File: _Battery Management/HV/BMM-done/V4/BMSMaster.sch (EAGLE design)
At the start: 119 parts, among them J1 M2_DF13-2P, J10 IMD, J14 USB_B_RA, J2 M2_DF13-2P, J3 M8S08B-PASK-2(LF)(SN), J5 M16_M_194280016, J6 M2770166, J7 M2770166, J8 M2770166, J9 M2770166, K1 ADJ14024, Q1 IRFR9120TRPBF, Q3 BSS123, U1 SN75HVD08DRMSOP, U10 NC7S14M5X, U11 LTC6820, U12 FT24C64A, U2 NCP1117DT_3.3, U22 NCV7805BDTRKG, U23 NUD3160DMT1G, U3 FT230X, U4 SN74LVC2G241, U5 NC7S14M5X, U6 DSPIC33FJ128GP804, U7 DMG6602SVTQ, U8 LTC6820, U9 MAX823TEUK+T_3.08, Y1 12Mhz

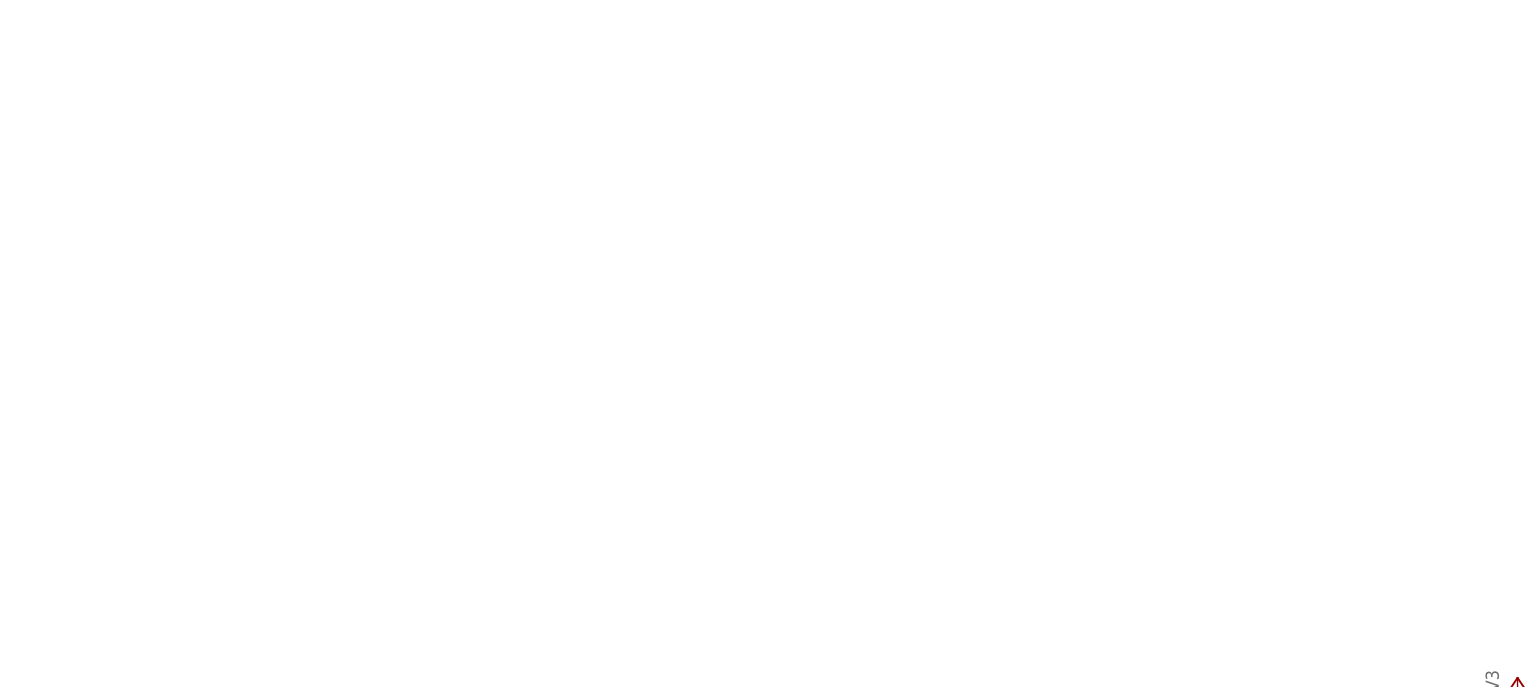
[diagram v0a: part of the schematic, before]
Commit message: Routing/ changing power supply
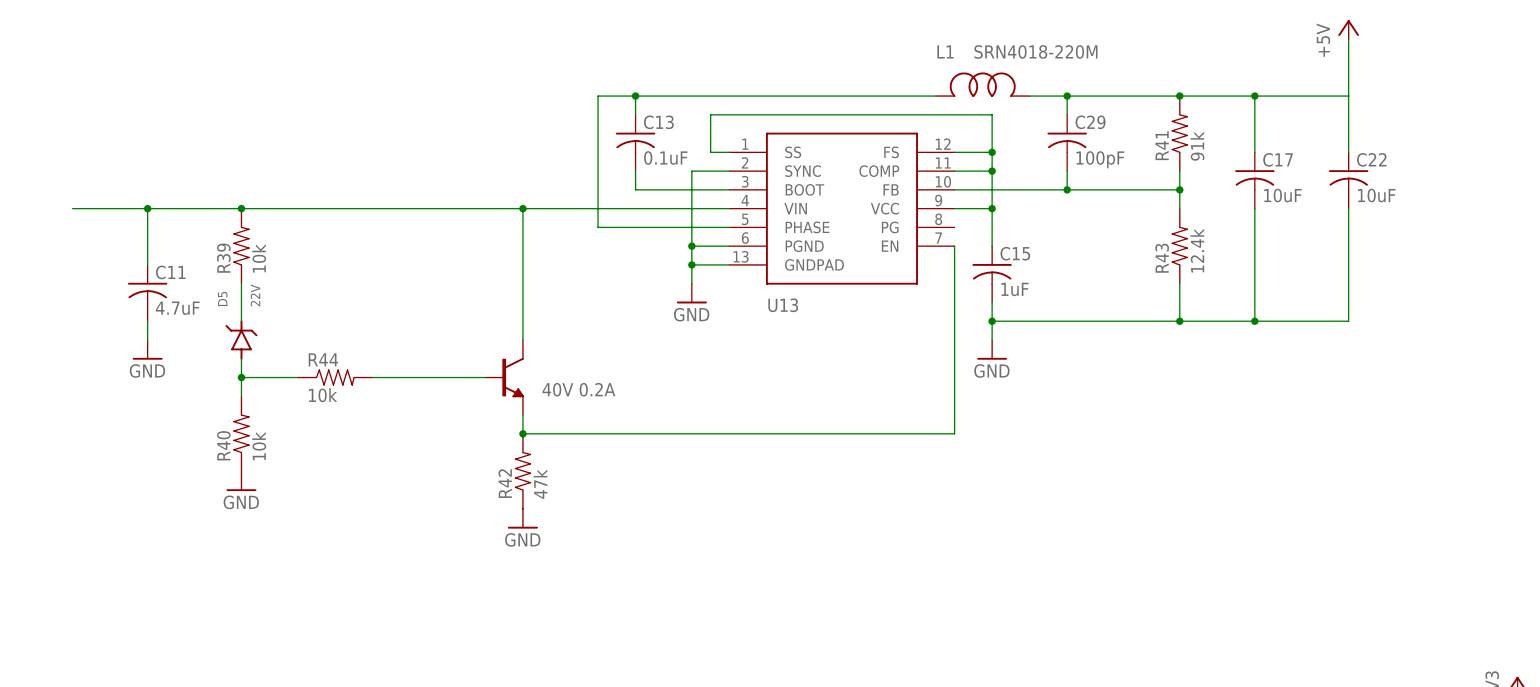
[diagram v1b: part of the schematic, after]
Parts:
- added C11: 4.7uF, FSAE Electric:CAP_4.7UF_50V
- added C13: 0.1uF, FSAE Electric:CAP_0.1UF_50V
- added C15: 1uF, FSAE Electric:CAP_1UF_50V_0805
- added C17, C22: 10uF, FSAE Electric:CAP_10UF_50V
- added C29: 100pF, FSAE Electric:CAP_100PF_50V
- added D5: 22V, FSAE Electric:DIODE-ZENER_22V
- added L1: SRN4018-220M, FSAE Electric:SRN4018-220M
- added Q2: 40V 0.2A, FSAE Electric:NPN_40V_0.2A
- added R39, R40, R44: 10k, FSAE Electric:RES_10K_1%
- added R41: 91k, FSAE Electric:RES_91K_1%_0805
- added R42: 47k, FSAE Electric:RES_47K_1%
- added R43: 12.4k, FSAE Electric:RES_12.4K_1%
- added U13: ISL85415-FRZ-T7A, FSAE Electric:ISL85415-FRZ-T7A
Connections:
- new net N$21: D5.A, R40.2, R44.1
- new net N$52: Q2.P$2, R42.2, U13.EN
- new net N$53: D5.C, R39.1
- new net N$55: C13.+, L1.P$1, U13.PHASE
- new net N$56: C13.-, U13.BOOT
- new net N$57: C15.+, U13.COMP, U13.FS, U13.SS, U13.VCC
- new net N$58: Q2.P$1, R44.2
- new net N$59: C11.+, Q2.P$3, R39.2, U13.VIN
- new net N$66: C29.-, R41.1, R43.2, U13.FB
- net +5V: now also C17.+, C22.+, C29.+, L1.P$2, R41.2
- net GND: now also C11.-, C15.-, C17.-, C22.-, R40.1, R42.1, R43.1, U13.GNDPAD, U13.PGND, U13.SYNC

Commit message: Trying to figure out DC/DC converter
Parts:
- removed C11: 4.7uF, FSAE Electric:CAP_4.7UF_50V
- removed C13: 0.1uF, FSAE Electric:CAP_0.1UF_50V
- removed C15: 1uF, FSAE Electric:CAP_1UF_50V_0805
- removed C17, C22: 10uF, FSAE Electric:CAP_10UF_50V
- removed C27, C28, C5, C6: 10UF, FSAE Electric:CAP-POL_10UF_16V
- removed C29: 100pF, FSAE Electric:CAP_100PF_50V
- removed D5: 22V, FSAE Electric:DIODE-ZENER_22V
- removed L1: SRN4018-220M, FSAE Electric:SRN4018-220M
- removed Q2: 40V 0.2A, FSAE Electric:NPN_40V_0.2A
- removed R39, R40, R44: 10k, FSAE Electric:RES_10K_1%
- removed R41: 91k, FSAE Electric:RES_91K_1%_0805
- removed R42: 47k, FSAE Electric:RES_47K_1%
- removed R43: 12.4k, FSAE Electric:RES_12.4K_1%
- removed U13: ISL85415-FRZ-T7A, FSAE Electric:ISL85415-FRZ-T7A
- removed U2: NCP1117DT_3.3, FSAE Electric:NCP1117DT_3.3
- removed U22: NCV7805BDTRKG, FSAE Electric:NCV7805BDTRKG
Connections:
- removed net N$21: D5.A, R40.2, R44.1
- removed net N$52: Q2.P$2, R42.2, U13.EN
- removed net N$53: D5.C, R39.1
- removed net N$55: C13.+, L1.P$1, U13.PHASE
- removed net N$56: C13.-, U13.BOOT
- removed net N$57: C15.+, U13.COMP, U13.FS, U13.SS, U13.VCC
- removed net N$58: Q2.P$1, R44.2
- removed net N$59: C11.+, Q2.P$3, R39.2, U13.VIN
- removed net N$66: C29.-, R41.1, R43.2, U13.FB
- new net N$60: L3.1
- net +3V3: no longer C28.+, U2.OUT
- net +5V: no longer C17.+, C22.+, C27.+, C29.+, L1.P$2, R41.2, U22.VO
- net +9V: no longer C5.+, C6.+, U2.IN, U22.VI
- net GND: no longer C11.-, C15.-, C17.-, C22.-, C27.-, C28.-, C5.-, C6.-, L3.1, R40.1, R42.1, R43.1, U13.GNDPAD, U13.PGND, U13.SYNC, U2.GND, U22.GND

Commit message: Adding parts and still routing
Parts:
- J1, J2: value M2_DF13-2P -> M2S02B-PASK-2(LF)(SN); device FSAE Electric:M2_DF13-2P -> FSAE Electric:M2S02B-PASK-2(LF)(SN)
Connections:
- removed net N$31: J5.6, K1G$2.C
- removed net N$32: J5.7, K1G$2.NC
- removed net N$59_N: J1.2, TX4.4
- removed net N$61_N: J2.2, TX3.4
- new net N$21: J5.6
- new net N$52: J5.7
- new net N$53: J2.2, TX4.6
- new net N$55: J2.1, TX4.4
- net N$33: now also J1.2, TX3.6; no longer J1.1, TX4.6
- net N$34: now also J1.1, TX3.4; no longer J2.1, TX3.6

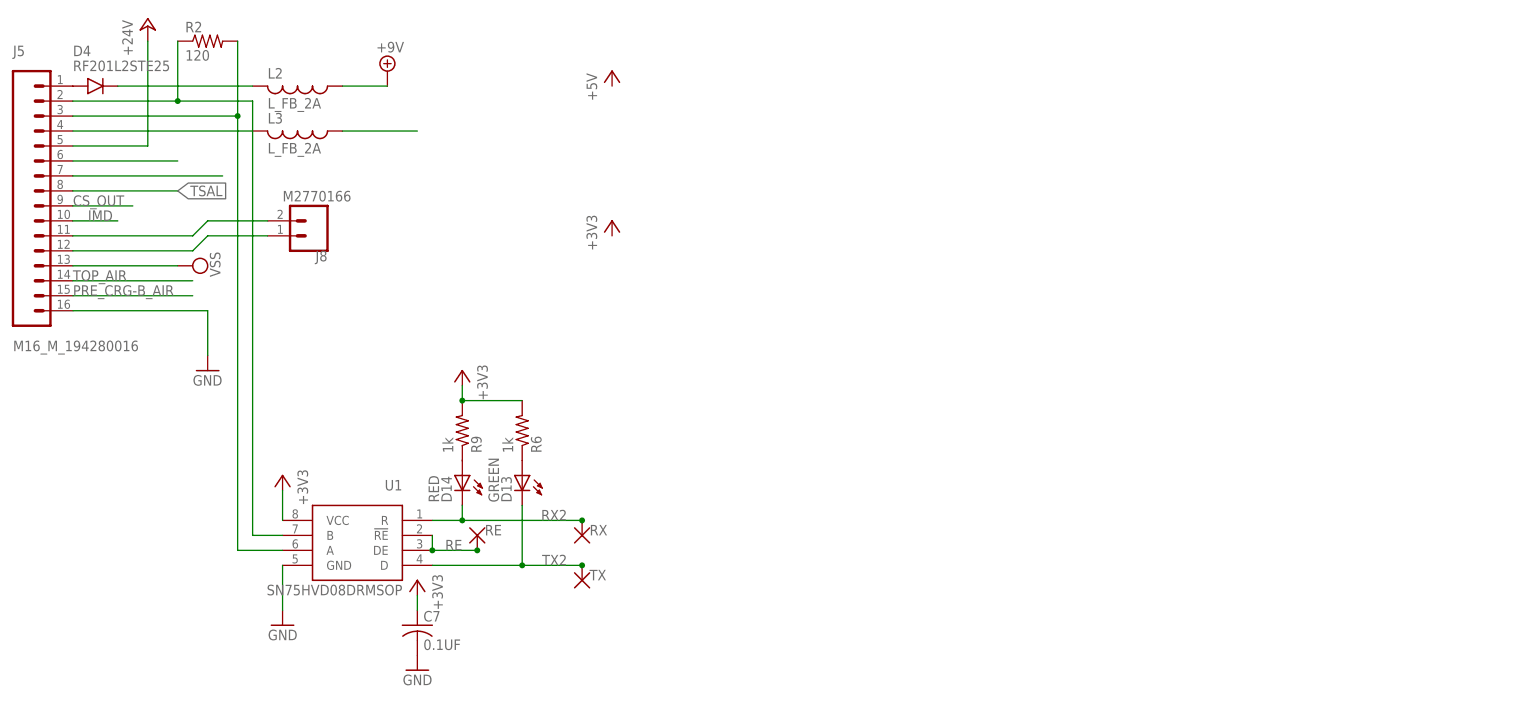
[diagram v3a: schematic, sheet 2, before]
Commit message: Working on DC/DC power supply
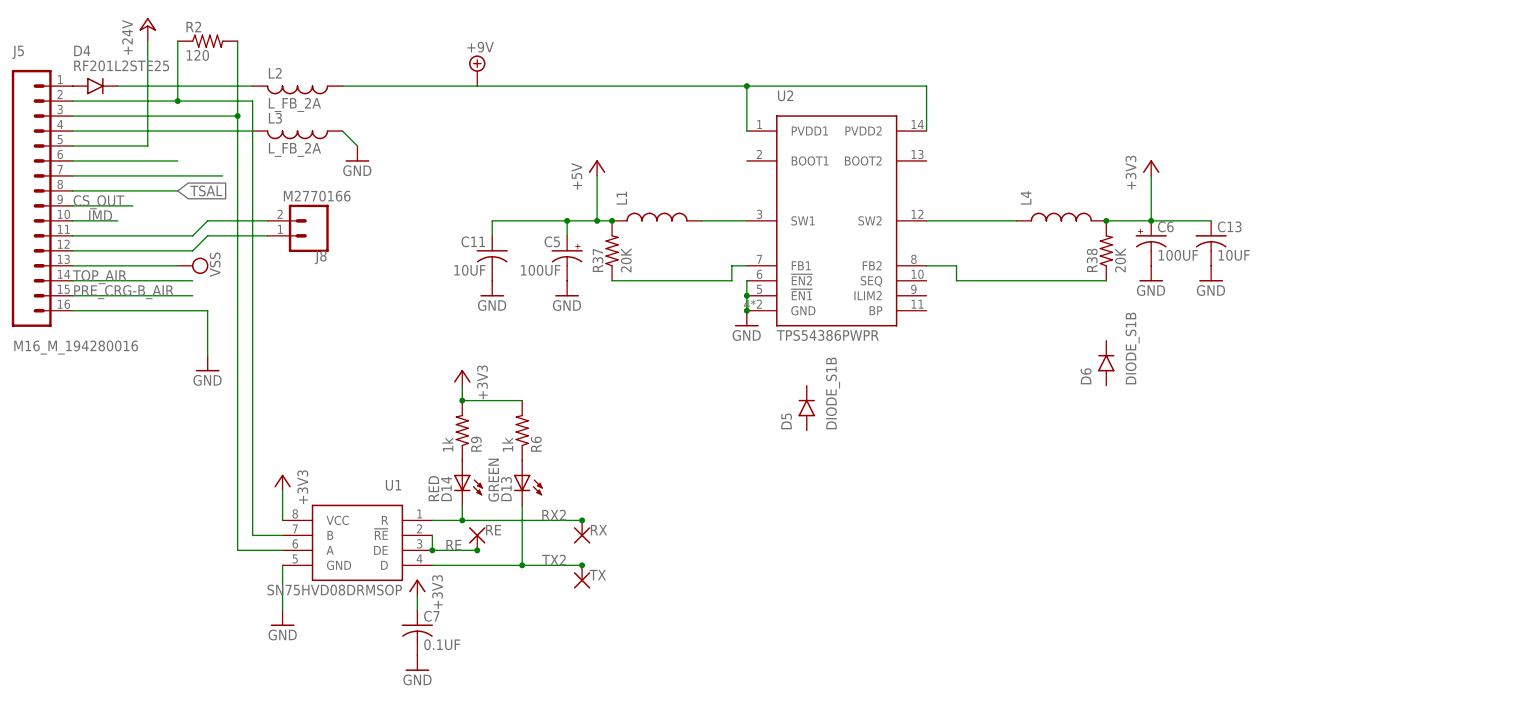
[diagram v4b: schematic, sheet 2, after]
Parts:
- added C11, C13: 10UF, FSAE Electric:CAP_10UF_50V
- added C5, C6: 100UF, FSAE Electric:CAP-POL_100UF_50V_SMD
- added D5, D6: DIODE_S1B, FSAE Electric:DIODE_S1B
- added L1, L4: (no value), FSAE Electric:INDUCTOR-220MR62
- added R37, R38: 20K, FSAE Electric:RES_20K_1%_0805
- added U2: TPS54386PWPR, FSAE Electric:TPS54386PWPR
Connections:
- removed net N$60: L3.1
- new net N$56: L1.2, U2.SW1
- new net N$57: L4.1, U2.SW2
- new net N$59: R37.1, U2.FB1
- new net N$61: R38.1, U2.FB2
- net +3V3: now also C13.+, C6.+, L4.2, R38.2
- net +5V: now also C11.+, C5.+, L1.1, R37.2
- net +9V: now also U2.PVDD1, U2.PVDD2
- net GND: now also C11.-, C13.-, C5.-, C6.-, L3.1, U2.!EN1, U2.!EN2, U2.GND
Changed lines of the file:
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@@
 <part name="J1" library="FSAE Electric" deviceset="M2" device="S02B-PASK-2(LF)(SN)"/>
 <part name="J2" library="FSAE Electric" deviceset="M2" device="S02B-PASK-2(LF)(SN)"/>
+<part name="U2" library="FSAE Electric" deviceset="TPS54386PWPR" device=""/>
+<part name="GND8" library="supply1" deviceset="GND" device=""/>
+<part name="GND32" library="supply1" deviceset="GND" device=""/>
+<part name="L1" library="FSAE Electric" deviceset="INDUCTOR" device="-220MR62"/>
+<part name="L4" library="FSAE Electric" deviceset="INDUCTOR" device="-220MR62"/>
+<part name="D5" library="FSAE Electric" deviceset="DIODE" device="_S1B"/>
+<part name="D6" library="FSAE Electric" deviceset="DIODE" device="_S1B"/>
+<part name="R37" library="FSAE Electric" deviceset="RES" device="_20K_1%_0805" value="20K"/>
+<part name="R38" library="FSAE Electric" deviceset="RES" device="_20K_1%_0805" value="20K"/>
+<part name="C5" library="FSAE Electric" deviceset="CAP-POL" device="_100UF_50V_SMD" value="100UF"/>
+<part name="C6" library="FSAE Electric" deviceset="CAP-POL" device="_100UF_50V_SMD" value="100UF"/>
+<part name="C11" library="FSAE Electric" deviceset="CAP" device="_10UF_50V" value="10UF"/>
+<part name="C13" library="FSAE Electric" deviceset="CAP" device="_10UF_50V" value="10UF"/>
+<part name="GND35" library="supply1" deviceset="GND" device=""/>
+<part name="GND36" library="supply1" deviceset="GND" device=""/>
+<part name="GND37" library="supply1" deviceset="GND" device=""/>
+<part name="GND39" library="supply1" deviceset="GND" device=""/>
 </parts>
 <sheets>
@@
 </plain>
 <instances>
-<instance part="P+18" gate="1" x="165.1" y="106.68"/>
-<instance part="SUPPLY11" gate="G$1" x="127" y="106.68"/>
+<instance part="P+18" gate="1" x="162.56" y="91.44"/>
+<instance part="SUPPLY11" gate="G$1" x="142.24" y="106.68"/>
 <instance part="GND4" gate="1" x="109.22" y="12.7" rot="MR0"/>
 <instance part="+3V4" gate="G$1" x="139.7" y="55.88" rot="MR0"/>
@@
 <instance part="R2" gate="G$1" x="96.52" y="111.76"/>
 <instance part="SUPPLY7" gate="G$1" x="93.98" y="73.66" rot="R90"/>
-<instance part="+3V9" gate="G$1" x="165.1" y="81.28"/>
+<instance part="+3V9" gate="G$1" x="256.54" y="91.44"/>
 <instance part="U1" gate="G$1" x="121.92" y="27.94" rot="MR0"/>
 <instance part="RE" gate="G$1" x="142.24" y="27.94" smashed="yes">
@@
 <attribute name="NAME" x="161.29" y="20.32" size="1.778" layer="95"/>
 </instance>
+<instance part="U2" gate="G$1" x="203.2" y="83.82"/>
+<instance part="GND8" gate="1" x="121.92" y="91.44"/>
+<instance part="GND32" gate="1" x="187.96" y="63.5"/>
+<instance part="L1" gate="G$1" x="172.72" y="81.28" rot="R90"/>
+<instance part="L4" gate="G$1" x="241.3" y="81.28" rot="R90"/>
+<instance part="D5" gate="G$1" x="198.12" y="48.26" rot="R90"/>
+<instance part="D6" gate="G$1" x="248.92" y="55.88" rot="R90"/>
+<instance part="R37" gate="G$1" x="165.1" y="76.2" rot="R90"/>
+<instance part="R38" gate="G$1" x="248.92" y="76.2" rot="R90"/>
+<instance part="C5" gate="G$1" x="157.48" y="76.2" rot="MR0"/>
+<instance part="C6" gate="G$1" x="256.54" y="78.74"/>
+<instance part="C11" gate="G$1" x="144.78" y="76.2" rot="MR0"/>
+<instance part="C13" gate="G$1" x="266.7" y="78.74"/>
+<instance part="GND35" gate="1" x="157.48" y="68.58"/>
+<instance part="GND36" gate="1" x="144.78" y="68.58"/>
+<instance part="GND37" gate="1" x="256.54" y="71.12"/>
+<instance part="GND39" gate="1" x="266.7" y="71.12"/>
 </instances>
 <busses>
@@
 <pinref part="C7" gate="G$1" pin="-"/>
 <pinref part="GND18" gate="1" pin="GND"/>
+</segment>
+<segment>
+<wire x1="121.92" y1="93.98" x2="119.38" y2="96.52" width="0.1524" layer="91"/>
+<pinref part="L3" gate="G$1" pin="1"/>
+<pinref part="GND8" gate="1" pin="GND"/>
+</segment>
+<segment>
+<pinref part="U2" gate="G$1" pin="GND"/>
+<pinref part="GND32" gate="1" pin="GND"/>
+<pinref part="U2" gate="G$1" pin="!EN2"/>
+<pinref part="U2" gate="G$1" pin="!EN1"/>
+<wire x1="187.96" y1="71.12" x2="187.96" y2="68.58" width="0.1524" layer="91"/>
+<wire x1="187.96" y1="68.58" x2="187.96" y2="66.04" width="0.1524" layer="91"/>
+<junction x="187.96" y="66.04"/>
+<junction x="187.96" y="68.58"/>
+</segment>
+<segment>
+<pinref part="C5" gate="G$1" pin="-"/>
+<pinref part="GND35" gate="1" pin="GND"/>
+</segment>
+<segment>
+<pinref part="C11" gate="G$1" pin="-"/>
+<pinref part="GND36" gate="1" pin="GND"/>
+</segment>
+<segment>
+<pinref part="C6" gate="G$1" pin="-"/>
+<pinref part="GND37" gate="1" pin="GND"/>
+</segment>
+<segment>
+<pinref part="C13" gate="G$1" pin="-"/>
+<pinref part="GND39" gate="1" pin="GND"/>
 </segment>
 </net>
@@
 <wire x1="132.08" y1="17.78" x2="132.08" y2="15.24" width="0.1524" layer="91"/>
 </segment>
+<segment>
+<pinref part="L4" gate="G$1" pin="2"/>
+<pinref part="R38" gate="G$1" pin="2"/>
+<pinref part="C6" gate="G$1" pin="+"/>
+<wire x1="248.92" y1="81.28" x2="256.54" y2="81.28" width="0.1524" layer="91"/>
+<pinref part="C13" gate="G$1" pin="+"/>
+<wire x1="256.54" y1="81.28" x2="266.7" y2="81.28" width="0.1524" layer="91"/>
+<junction x="248.92" y="81.28"/>
+<junction x="256.54" y="81.28"/>
+<pinref part="+3V9" gate="G$1" pin="+3V3"/>
+<wire x1="256.54" y1="81.28" x2="256.54" y2="88.9" width="0.1524" layer="91"/>
+</segment>
 </net>
 <net name="+9V" class="0">
@@
 <pinref part="SUPPLY11" gate="G$1" pin="+9V"/>
 <pinref part="L2" gate="G$1" pin="1"/>
-<wire x1="127" y1="104.14" x2="119.38" y2="104.14" width="0.1524" layer="91"/>
+<wire x1="142.24" y1="104.14" x2="119.38" y2="104.14" width="0.1524" layer="91"/>
+<wire x1="142.24" y1="104.14" x2="187.96" y2="104.14" width="0.1524" layer="91"/>
+<wire x1="187.96" y1="104.14" x2="187.96" y2="96.52" width="0.1524" layer="91"/>
+<pinref part="U2" gate="G$1" pin="PVDD1"/>
+<pinref part="U2" gate="G$1" pin="PVDD2"/>
+<wire x1="187.96" y1="104.14" x2="218.44" y2="104.14" width="0.1524" layer="91"/>
+<wire x1="218.44" y1="104.14" x2="218.44" y2="96.52" width="0.1524" layer="91"/>
+<junction x="187.96" y="104.14"/>
 </segment>
 </net>
@@
 </segment>
 </net>
-<net name="N$60" class="0">
-<segment>
-<wire x1="132.08" y1="96.52" x2="119.38" y2="96.52" width="0.1524" layer="91"/>
-<pinref part="L3" gate="G$1" pin="1"/>
-</segment>
-</net>
+<net name="N$56" class="0">
+<segment>
+<pinref part="U2" gate="G$1" pin="SW1"/>
+<pinref part="L1" gate="G$1" pin="2"/>
+<wire x1="180.34" y1="81.28" x2="187.96" y2="81.28" width="0.1524" layer="91"/>
+</segment>
+</net>
+<net name="N$57" class="0">
+<segment>
+<pinref part="U2" gate="G$1" pin="SW2"/>
+<pinref part="L4" gate="G$1" pin="1"/>
+<wire x1="233.68" y1="81.28" x2="218.44" y2="81.28" width="0.1524" layer="91"/>
+</segment>
+</net>
+<net name="+5V" class="0">
+<segment>
+<pinref part="L1" gate="G$1" pin="1"/>
+<pinref part="R37" gate="G$1" pin="2"/>
+<pinref part="C11" gate="G$1" pin="+"/>
+<wire x1="165.1" y1="81.28" x2="162.56" y2="81.28" width="0.1524" layer="91"/>
+<wire x1="162.56" y1="81.28" x2="157.48" y2="81.28" width="0.1524" layer="91"/>
+<wire x1="157.48" y1="81.28" x2="144.78" y2="81.28" width="0.1524" layer="91"/>
+<wire x1="144.78" y1="81.28" x2="144.78" y2="78.74" width="0.1524" layer="91"/>
+<pinref part="C5" gate="G$1" pin="+"/>
+<wire x1="157.48" y1="78.74" x2="157.48" y2="81.28" width="0.1524" layer="91"/>
+<pinref part="P+18" gate="1" pin="+5V"/>
+<wire x1="162.56" y1="88.9" x2="162.56" y2="81.28" width="0.1524" layer="91"/>
+<junction x="165.1" y="81.28"/>
+<junction x="162.56" y="81.28"/>
+<junction x="157.48" y="81.28"/>
+</segment>
+</net>
+<net name="N$59" class="0">
+<segment>
+<pinref part="U2" gate="G$1" pin="FB1"/>
+<wire x1="187.96" y1="73.66" x2="185.42" y2="73.66" width="0.1524" layer="91"/>
+<wire x1="185.42" y1="73.66" x2="185.42" y2="71.12" width="0.1524" layer="91"/>
+<pinref part="R37" gate="G$1" pin="1"/>
+<wire x1="185.42" y1="71.12" x2="165.1" y2="71.12" width="0.1524" layer="91"/>
+</segment>
+</net>
+<net name="N$61" class="0">
+<segment>
+<pinref part="U2" gate="G$1" pin="FB2"/>
+<wire x1="218.44" y1="73.66" x2="223.52" y2="73.66" width="0.1524" layer="91"/>
+<wire x1="223.52" y1="73.66" x2="223.52" y2="71.12" width="0.1524" layer="91"/>
+<pinref part="R38" gate="G$1" pin="1"/>
+<wire x1="223.52" y1="71.12" x2="248.92" y2="71.12" width="0.1524" layer="91"/>
+</segment>
+</net>
